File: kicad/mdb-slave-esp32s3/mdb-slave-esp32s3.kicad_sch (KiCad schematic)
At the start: 38 parts, among them J1 MDB_Connector, J2 USB_C_Receptacle_USB2.0_16P, J3 Conn_02x11_Odd_Even, SW1 SW_Push, U1 TLP785, U3 ESP32-S3FH4R2, U4 TLP785, U5 LM2594HVM-3.3, Y1 Crystal_GND24

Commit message: Routing
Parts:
- added TP1: TestPoint, TestPoint:TestPoint_Pad_D1.0mm, symbol Connector:TestPoint
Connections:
- net vin: now also TP1.1
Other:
- moved on the sheet: TP4
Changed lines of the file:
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@@
 	)
 	(junction
+		(at 358.14 172.72)
+		(diameter 0)
+		(color 0 0 0 0)
+	)
+	(junction
 		(at 124.46 90.17)
 		(diameter 0)
@@
 		(color 0 0 0 0)
 	)
+	(junction
+		(at 288.29 170.18)
+		(diameter 0)
+		(color 0 0 0 0)
+	)
 	(no_connect
 		(at 231.14 185.42)
@@
 	(wire
 		(pts
-			(xy 29.21 99.06) (xy 31.75 99.06)
+			(xy 290.83 170.18) (xy 304.8 170.18)
 		)
 		(stroke
@@
 	(wire
 		(pts
-			(xy 290.83 170.18) (xy 304.8 170.18)
+			(xy 29.21 99.06) (xy 31.75 99.06)
 		)
 		(stroke
@@
 	(wire
 		(pts
-			(xy 283.21 170.18) (xy 290.83 170.18)
+			(xy 283.21 170.18) (xy 288.29 170.18)
 		)
 		(stroke
@@
 	(wire
 		(pts
-			(xy 356.87 172.72) (xy 351.79 172.72)
+			(xy 368.3 172.72) (xy 358.14 172.72)
 		)
 		(stroke
@@
 	(wire
 		(pts
+			(xy 288.29 170.18) (xy 290.83 170.18)
+		)
+		(stroke
+			(width 0)
+			(type default)
+		)
+	)
+	(wire
+		(pts
 			(xy 90.17 121.92) (xy 91.44 121.92)
 		)
@@
 	(wire
 		(pts
+			(xy 358.14 172.72) (xy 351.79 172.72)
+		)
+		(stroke
+			(width 0)
+			(type default)
+		)
+	)
+	(wire
+		(pts
 			(xy 356.87 105.41) (xy 358.14 105.41)
 		)
@@
 	(wire
 		(pts
-			(xy 78.74 38.1) (xy 78.74 36.83)
-		)
-		(stroke
-			(width 0)
-			(type default)
-		)
-	)
-	(wire
-		(pts
 			(xy 78.74 104.14) (xy 78.74 106.68)
 		)
@@
 	)
 	(symbol
+		(lib_id "Connector:TestPoint")
+		(at 288.29 170.18 0)
+		(unit 1)
+		(exclude_from_sim no)
+		(in_bom yes)
+		(on_board yes)
+		(dnp no)
+		(fields_autoplaced yes)
+		(property "Reference" "TP1"
+			(at 290.83 165.6079 0)
+			(effects
+				(font
+					(size 1.27 1.27)
+				)
+				(justify left)
+			)
+		)
+		(property "Value" "TestPoint"
+			(at 290.83 168.1479 0)
+			(effects
+				(font
+					(size 1.27 1.27)
+				)
+				(justify left)
+			)
+		)
+		(property "Footprint" "TestPoint:TestPoint_Pad_D1.0mm"
+			(at 293.37 170.18 0)
+			(effects
+				(font
+					(size 1.27 1.27)
+				)
+				(hide yes)
+			)
+		)
+		(property "Datasheet" "~"
+			(at 293.37 170.18 0)
+			(effects
+				(font
+					(size 1.27 1.27)
+				)
+				(hide yes)
+			)
+		)
+		(property "Description" "test point"
+			(at 288.29 170.18 0)
+			(effects
+				(font
+					(size 1.27 1.27)
+				)
+				(hide yes)
+			)
+		)
+		(pin "1"
+		)
+		(instances
+			(project "mdb-slave-esp32s3"
+				(path "/95980b25-0707-441d-ba83-7f6c6e1d1aaa"
+					(reference "TP1")
+					(unit 1)
+				)
+			)
+		)
+	)
+	(symbol
 		(lib_id "Device:R")
 		(at 175.26 114.3 90)
@@
 	(symbol
 		(lib_id "Connector:TestPoint")
-		(at 78.74 36.83 0)
+		(at 358.14 172.72 0)
 		(unit 1)
 		(exclude_from_sim no)
@@
 		(fields_autoplaced yes)
 		(property "Reference" "TP4"
-			(at 81.28 32.2579 0)
+			(at 360.68 168.1479 0)
 			(effects
 				(font
@@
 		)
 		(property "Value" "TestPoint"
-			(at 81.28 34.7979 0)
+			(at 360.68 170.6879 0)
 			(effects
 				(font
@@
 		)
 		(property "Footprint" "TestPoint:TestPoint_Pad_D1.0mm"
-			(at 83.82 36.83 0)
+			(at 363.22 172.72 0)
 			(effects
 				(font
@@
 		)
 		(property "Datasheet" "~"
-			(at 83.82 36.83 0)
+			(at 363.22 172.72 0)
 			(effects
 				(font
@@
 		)
 		(property "Description" "test point"
-			(at 78.74 36.83 0)
+			(at 358.14 172.72 0)
 			(effects
 				(font
@@
 	(symbol
 		(lib_id "power:+3V3")
-		(at 356.87 172.72 270)
+		(at 368.3 172.72 270)
 		(unit 1)
 		(exclude_from_sim no)
@@
 		(fields_autoplaced yes)
 		(property "Reference" "#PWR041"
-			(at 353.06 172.72 0)
+			(at 364.49 172.72 0)
 			(effects
 				(font
@@
 		)
 		(property "Value" "+3V3"
-			(at 360.68 172.7199 90)
+			(at 372.11 172.7199 90)
 			(effects
 				(font
@@
 		)
 		(property "Footprint" ""
-			(at 356.87 172.72 0)
+			(at 368.3 172.72 0)
 			(effects
 				(font
@@
 		)
 		(property "Datasheet" ""
-			(at 356.87 172.72 0)
+			(at 368.3 172.72 0)
 			(effects
 				(font
@@
 		)
 		(property "Description" ""
-			(at 356.87 172.72 0)
+			(at 368.3 172.72 0)
 			(effects
 				(font
@@
 					(unit 1)
 				)
-			)
-		)
-	)
-	(symbol
-		(lib_id "power:+3V3")
-		(at 78.74 38.1 180)
-		(unit 1)
-		(exclude_from_sim no)
-		(in_bom yes)
-		(on_board yes)
-		(dnp no)
-		(fields_autoplaced yes)
-		(property "Reference" "#PWR032"
-			(at 78.74 34.29 0)
-			(effects
-				(font
-					(size 1.27 1.27)
-				)
-				(hide yes)
-			)
-		)
-		(property "Value" "+3V3"
-			(at 78.74 43.18 0)
-			(effects
-				(font
-					(size 1.27 1.27)
-				)
-			)
-		)
-		(property "Footprint" ""
-			(at 78.74 38.1 0)
-			(effects
-				(font
-					(size 1.27 1.27)
-				)
-				(hide yes)
-			)
-		)
-		(property "Datasheet" ""
-			(at 78.74 38.1 0)
-			(effects
-				(font
-					(size 1.27 1.27)
-				)
-				(hide yes)
-			)
-		)
-		(property "Description" ""
-			(at 78.74 38.1 0)
-			(effects
-				(font
-					(size 1.27 1.27)
-				)
-				(hide yes)
-			)
-		)
-		(pin "1"
-		)
-		(instances
-			(project "mdb-slave-esp32s3"
-				(path "/95980b25-0707-441d-ba83-7f6c6e1d1aaa"
-					(reference "#PWR032")
-					(unit 1)
-				)

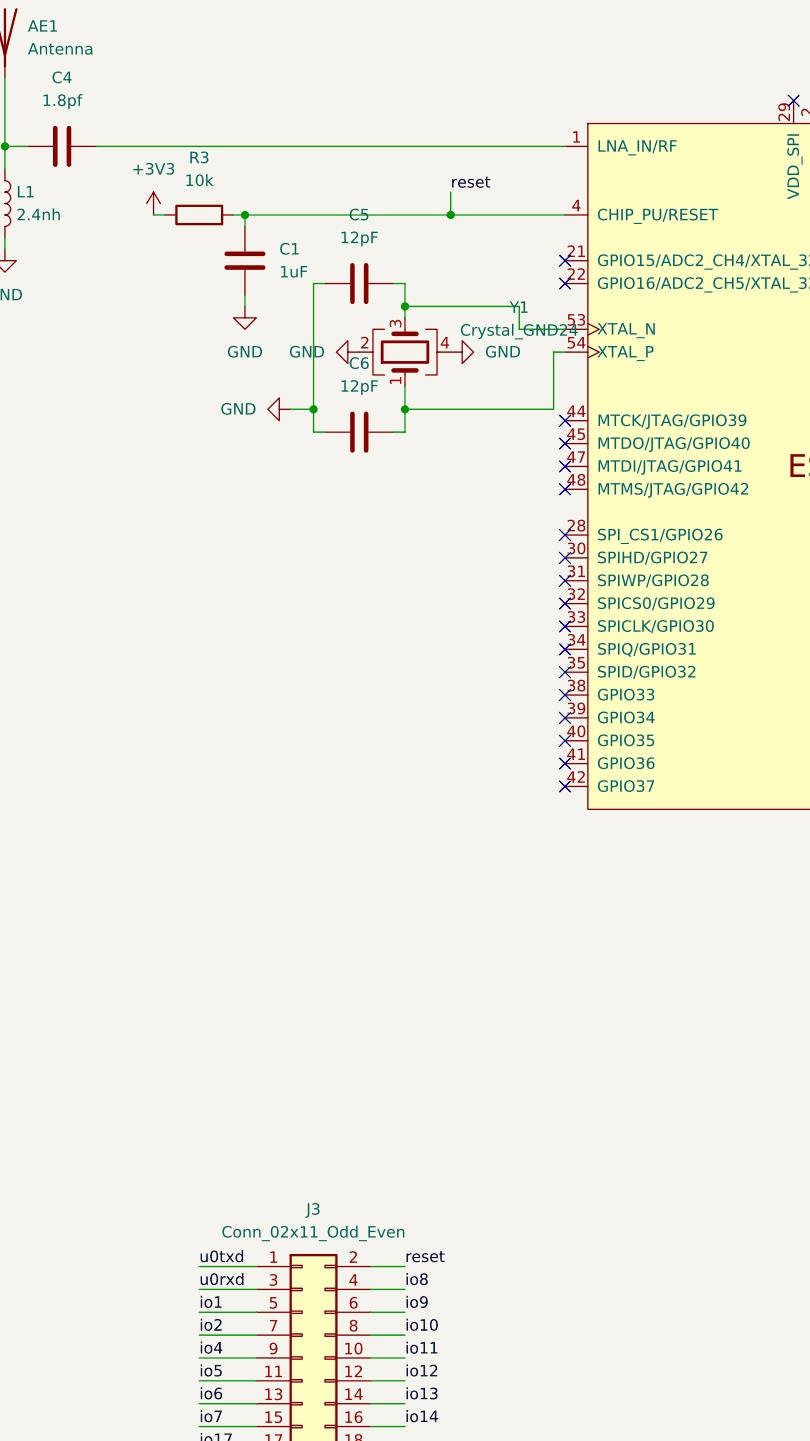
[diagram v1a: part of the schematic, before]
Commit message: Refacting production components
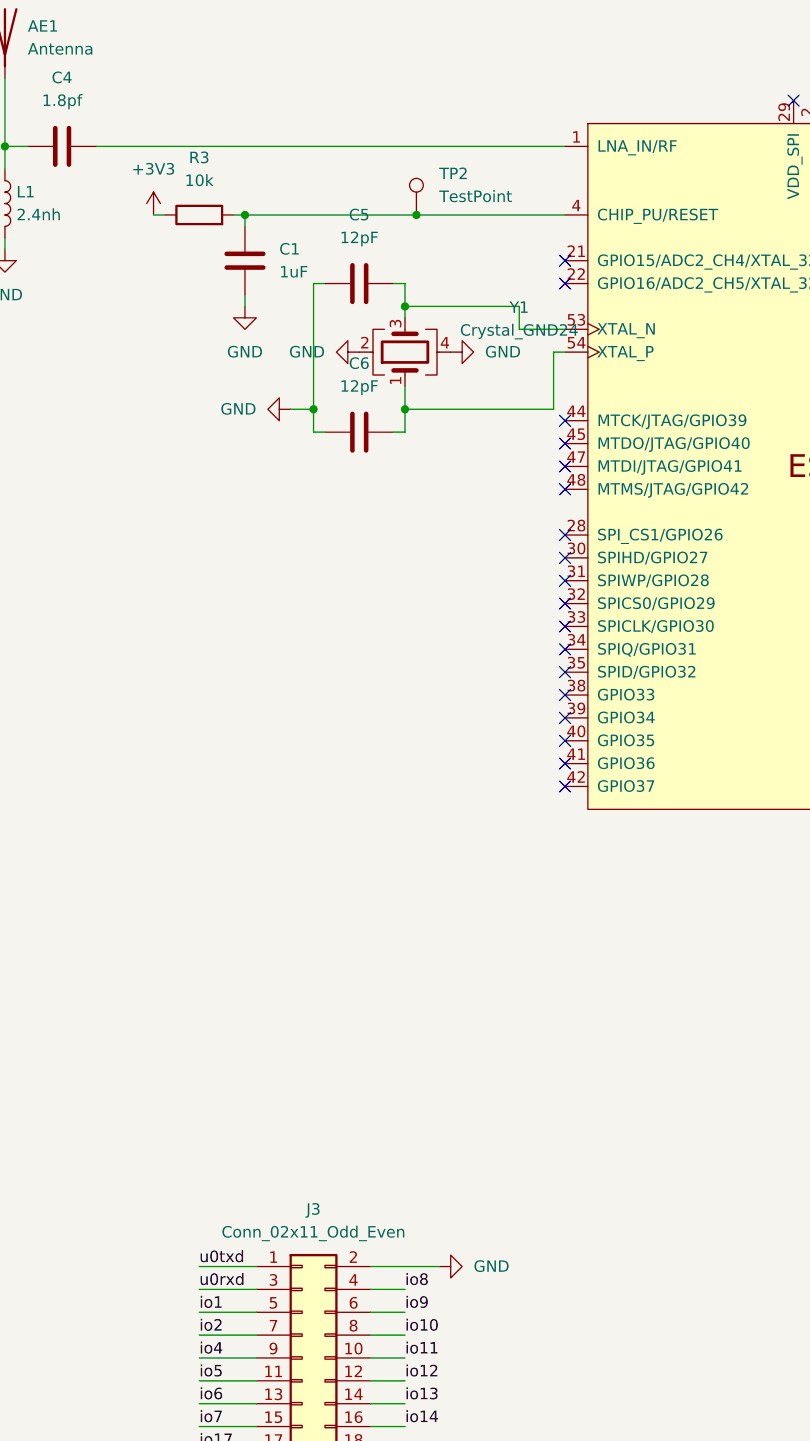
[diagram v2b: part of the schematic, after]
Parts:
- added TP2: TestPoint, TestPoint:TestPoint_Pad_D1.0mm, symbol Connector:TestPoint
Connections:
- net GND: now also J3.2 (Pin_2)
- net reset: no longer names the net of C1.1, R3.2, U3.4 (CHIP_PU/RESET)
- net reset: now also TP2.1; no longer J3.2 (Pin_2)
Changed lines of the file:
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@@
 	)
 	(junction
-		(at 78.74 106.68)
+		(at 231.14 177.8)
 		(diameter 0)
 		(color 0 0 0 0)
 	)
 	(junction
-		(at 231.14 177.8)
+		(at 73.66 128.27)
 		(diameter 0)
 		(color 0 0 0 0)
 	)
 	(junction
-		(at 73.66 128.27)
+		(at 74.93 106.68)
 		(diameter 0)
 		(color 0 0 0 0)
@@
 	(wire
 		(pts
-			(xy 157.48 157.48) (xy 160.02 157.48)
+			(xy 74.93 106.68) (xy 91.44 106.68)
 		)
 		(stroke
@@
 	(wire
 		(pts
-			(xy 203.2 246.38) (xy 203.2 243.84)
+			(xy 157.48 157.48) (xy 160.02 157.48)
 		)
 		(stroke
@@
 	(wire
 		(pts
-			(xy 55.88 107.95) (xy 55.88 106.68)
+			(xy 203.2 246.38) (xy 203.2 243.84)
 		)
 		(stroke
@@
 	(wire
 		(pts
-			(xy 186.69 236.22) (xy 195.58 236.22)
+			(xy 55.88 107.95) (xy 55.88 106.68)
 		)
 		(stroke
@@
 	(wire
 		(pts
-			(xy 72.39 114.3) (xy 73.66 114.3)
+			(xy 186.69 236.22) (xy 195.58 236.22)
 		)
 		(stroke
@@
 	(wire
 		(pts
-			(xy 201.93 30.48) (xy 201.93 33.02)
+			(xy 72.39 114.3) (xy 73.66 114.3)
 		)
 		(stroke
@@
 	(wire
 		(pts
-			(xy 73.66 226.06) (xy 69.85 226.06)
+			(xy 201.93 30.48) (xy 201.93 33.02)
 		)
 		(stroke
@@
 	(wire
 		(pts
-			(xy 158.75 30.48) (xy 175.26 30.48)
+			(xy 73.66 226.06) (xy 69.85 226.06)
 		)
 		(stroke
@@
 	(wire
 		(pts
-			(xy 78.74 106.68) (xy 91.44 106.68)
+			(xy 158.75 30.48) (xy 175.26 30.48)
 		)
 		(stroke
@@
 	(wire
 		(pts
-			(xy 55.88 106.68) (xy 78.74 106.68)
+			(xy 55.88 106.68) (xy 74.93 106.68)
 		)
 		(stroke
@@
 	(wire
 		(pts
-			(xy 73.66 223.52) (xy 69.85 223.52)
+			(xy 77.47 223.52) (xy 69.85 223.52)
 		)
 		(stroke
@@
 	(wire
 		(pts
-			(xy 78.74 104.14) (xy 78.74 106.68)
-		)
-		(stroke
-			(width 0)
-			(type default)
-		)
-	)
-	(wire
-		(pts
 			(xy 231.14 170.18) (xy 231.14 172.72)
 		)
@@
 		)
 	)
-	(label "reset"
-		(at 78.74 104.14 0)
-		(effects
-			(font
-				(size 1.27 1.27)
-			)
-			(justify left bottom)
-		)
-	)
 	(label "io18"
 		(at 50.8 246.38 0)
@@
 		)
 	)
-	(label "reset"
-		(at 73.66 223.52 0)
-		(effects
-			(font
-				(size 1.27 1.27)
-			)
-			(justify left bottom)
-		)
-	)
 	(label "boot"
 		(at 160.02 113.03 0)
@@
 	)
 	(symbol
+		(lib_id "Connector:TestPoint")
+		(at 74.93 106.68 0)
+		(unit 1)
+		(exclude_from_sim no)
+		(in_bom yes)
+		(on_board yes)
+		(dnp no)
+		(fields_autoplaced yes)
+		(property "Reference" "TP2"
+			(at 77.47 102.1079 0)
+			(effects
+				(font
+					(size 1.27 1.27)
+				)
+				(justify left)
+			)
+		)
+		(property "Value" "TestPoint"
+			(at 77.47 104.6479 0)
+			(effects
+				(font
+					(size 1.27 1.27)
+				)
+				(justify left)
+			)
+		)
+		(property "Footprint" "TestPoint:TestPoint_Pad_D1.0mm"
+			(at 80.01 106.68 0)
+			(effects
+				(font
+					(size 1.27 1.27)
+				)
+				(hide yes)
+			)
+		)
+		(property "Datasheet" "~"
+			(at 80.01 106.68 0)
+			(effects
+				(font
+					(size 1.27 1.27)
+				)
+				(hide yes)
+			)
+		)
+		(property "Description" "test point"
+			(at 74.93 106.68 0)
+			(effects
+				(font
+					(size 1.27 1.27)
+				)
+				(hide yes)
+			)
+		)
+		(pin "1"
+		)
+		(instances
+			(project "mdb-slave-esp32s3"
+				(path "/95980b25-0707-441d-ba83-7f6c6e1d1aaa"
+					(reference "TP2")
+					(unit 1)
+				)
+			)
+		)
+	)
+	(symbol
 		(lib_id "Graphic:Logo_Open_Hardware_Small")
 		(at 35.56 35.56 0)
@@
 					(unit 1)
 				)
+			)
+		)
+	)
+	(symbol
+		(lib_id "power:GND")
+		(at 77.47 223.52 90)
+		(unit 1)
+		(exclude_from_sim no)
+		(in_bom yes)
+		(on_board yes)
+		(dnp no)
+		(fields_autoplaced yes)
+		(property "Reference" "#PWR031"
+			(at 83.82 223.52 0)
+			(effects
+				(font
+					(size 1.27 1.27)
+				)
+				(hide yes)
+			)
+		)
+		(property "Value" "GND"
+			(at 81.28 223.52 90)
+			(effects
+				(font
+					(size 1.27 1.27)
+				)
+				(justify right)
+			)
+		)
+		(property "Footprint" ""
+			(at 77.47 223.52 0)
+			(effects
+				(font
+					(size 1.27 1.27)
+				)
+				(hide yes)
+			)
+		)
+		(property "Datasheet" ""
+			(at 77.47 223.52 0)
+			(effects
+				(font
+					(size 1.27 1.27)
+				)
+				(hide yes)
+			)
+		)
+		(property "Description" ""
+			(at 77.47 223.52 0)
+			(effects
+				(font
+					(size 1.27 1.27)
+				)
+				(hide yes)
+			)
+		)
+		(pin "1"
+		)
+		(instances
+			(project "mdb-slave-esp32s3"
+				(path "/95980b25-0707-441d-ba83-7f6c6e1d1aaa"
+					(reference "#PWR031")
+					(unit 1)
+				)

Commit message: updating production components
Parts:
- TP1, TP2, TP4: now left out of the parts list
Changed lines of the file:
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@@
 		(unit 1)
 		(exclude_from_sim no)
-		(in_bom yes)
+		(in_bom no)
 		(on_board yes)
 		(dnp no)
@@
 		(unit 1)
 		(exclude_from_sim no)
-		(in_bom yes)
+		(in_bom no)
 		(on_board yes)
 		(dnp no)
@@
 		(unit 1)
 		(exclude_from_sim no)
-		(in_bom yes)
-		(on_board yes)
-		(dnp no)
+		(in_bom no)
+		(on_board yes)
+		(dnp no)

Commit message: MDB socket angle
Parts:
- J1: LCSC# C22365701 -> C22365656; LCSC2# (none) -> C22365701
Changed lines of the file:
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@@
 			)
 		)
-		(property "LCSC#" "C22365701"
+		(property "LCSC#" "C22365656"
 			(at 356.87 68.58 0)
 			(effects
+				(font
+					(size 1.27 1.27)
+				)
+				(hide yes)
+			)
+		)
+		(property "LCSC2#" "C22365701"
+			(at 356.87 68.58 0)
+			(effects

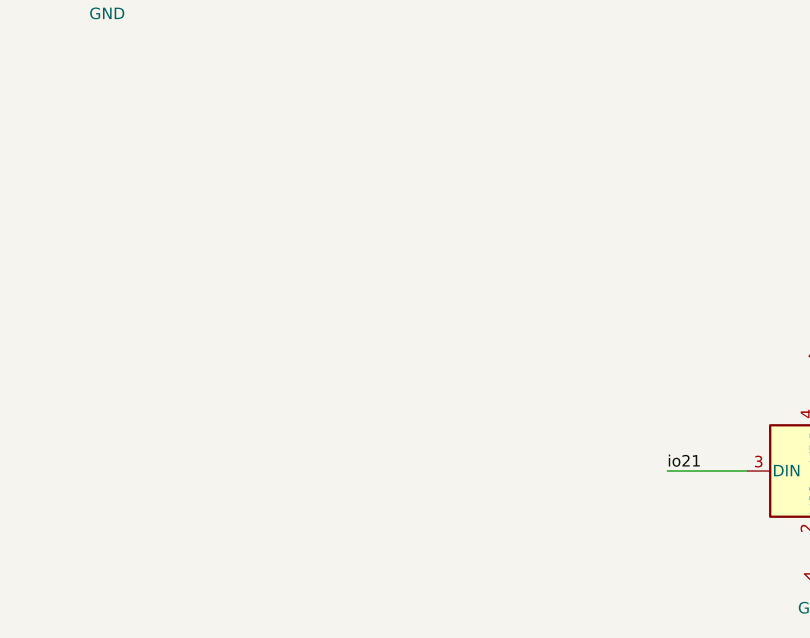
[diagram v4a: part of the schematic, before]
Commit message: Adding NTC thermal sensor
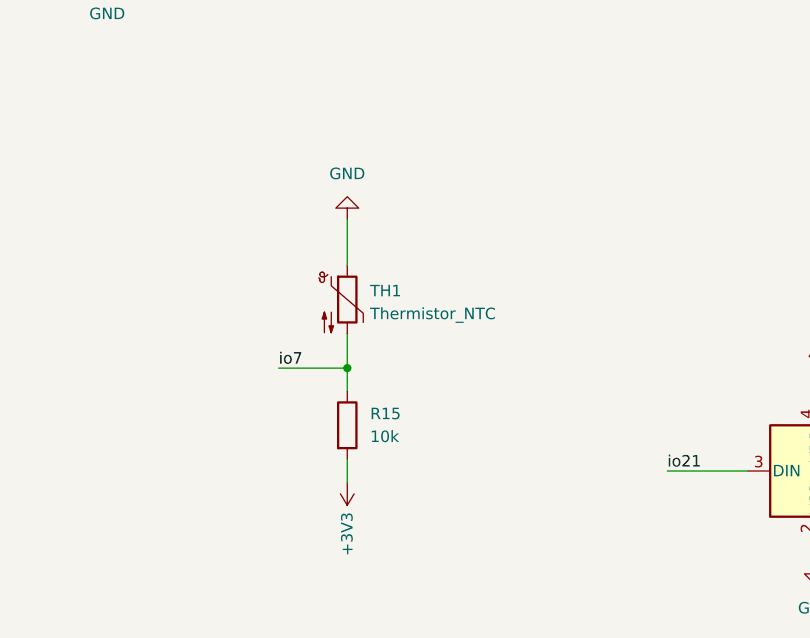
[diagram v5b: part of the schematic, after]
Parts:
- added R15: 10k, Resistor_SMD:R_0603_1608Metric, symbol Device:R
- added TH1: Thermistor_NTC, Resistor_SMD:R_0603_1608Metric, symbol Device:Thermistor_NTC
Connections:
- net +3V3: now also R15.2
- net GND: now also TH1.1
- net io7: now also R15.1, TH1.2

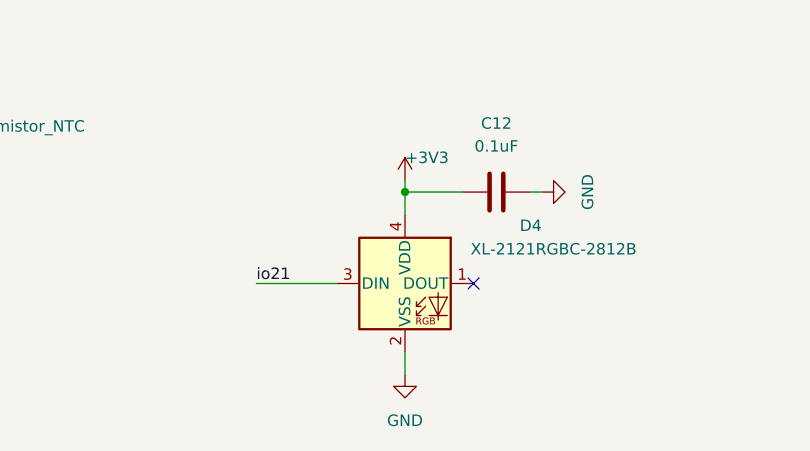
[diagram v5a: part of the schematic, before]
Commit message: Updating LED footprint
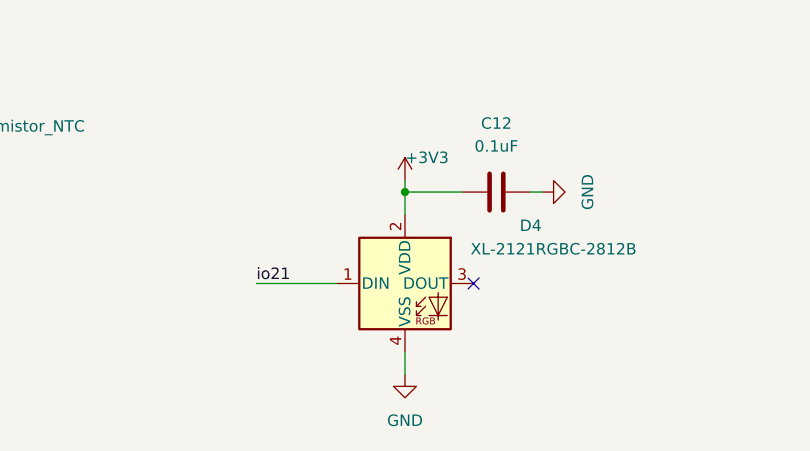
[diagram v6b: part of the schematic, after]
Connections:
- net +3V3: now also D4.2 (VDD); no longer D4.4 (VDD)
- net GND: now also D4.4 (VSS); no longer D4.2 (VSS)
- net io21: now also D4.1 (DIN); no longer D4.3 (DIN)
